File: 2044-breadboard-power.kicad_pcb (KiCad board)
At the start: 2 copper layers, 51 x 22 mm, 13 parts, among them J1 Conn_02x02_Odd_Even, J2 PJ-102AH, J3 Conn_02x02_Odd_Even, U1 AZ1117CH-3.3TRG1, U2 AZ1117CH-5.0TRG1

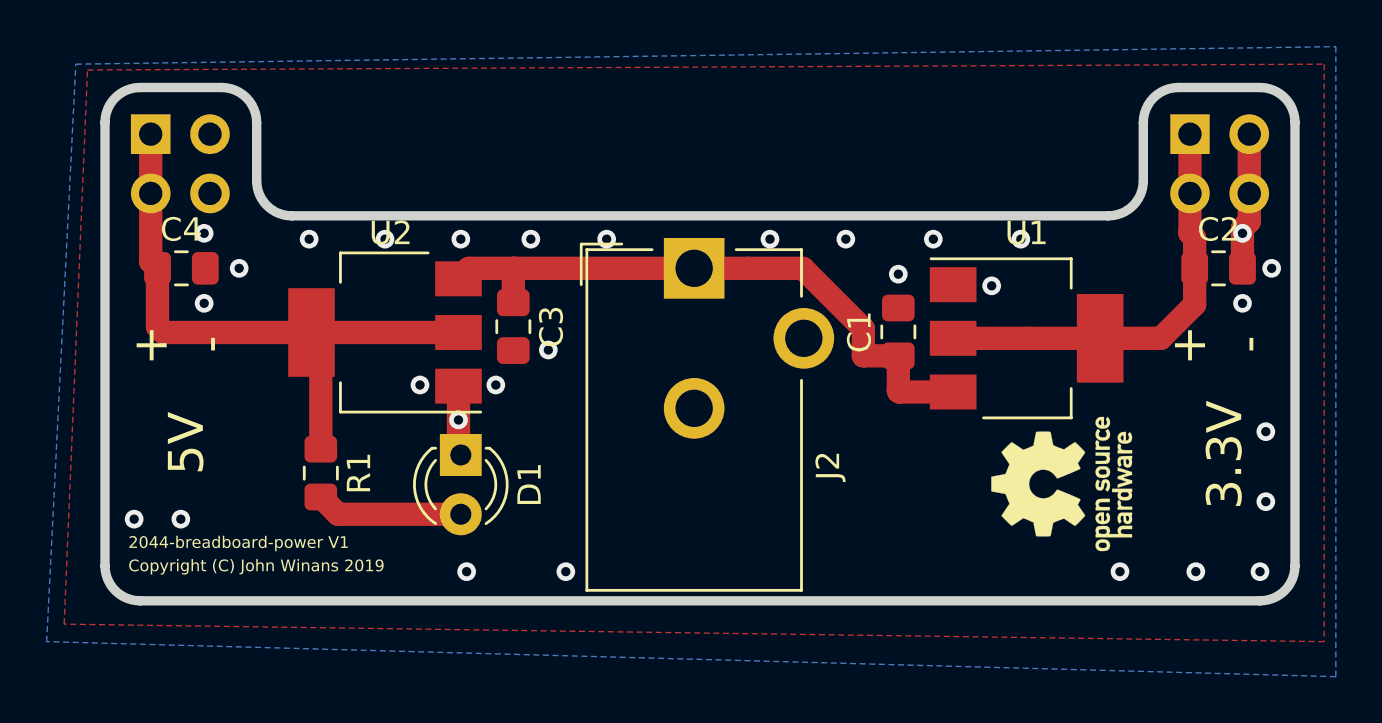
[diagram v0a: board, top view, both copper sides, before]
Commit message: Add ground on the output headers.
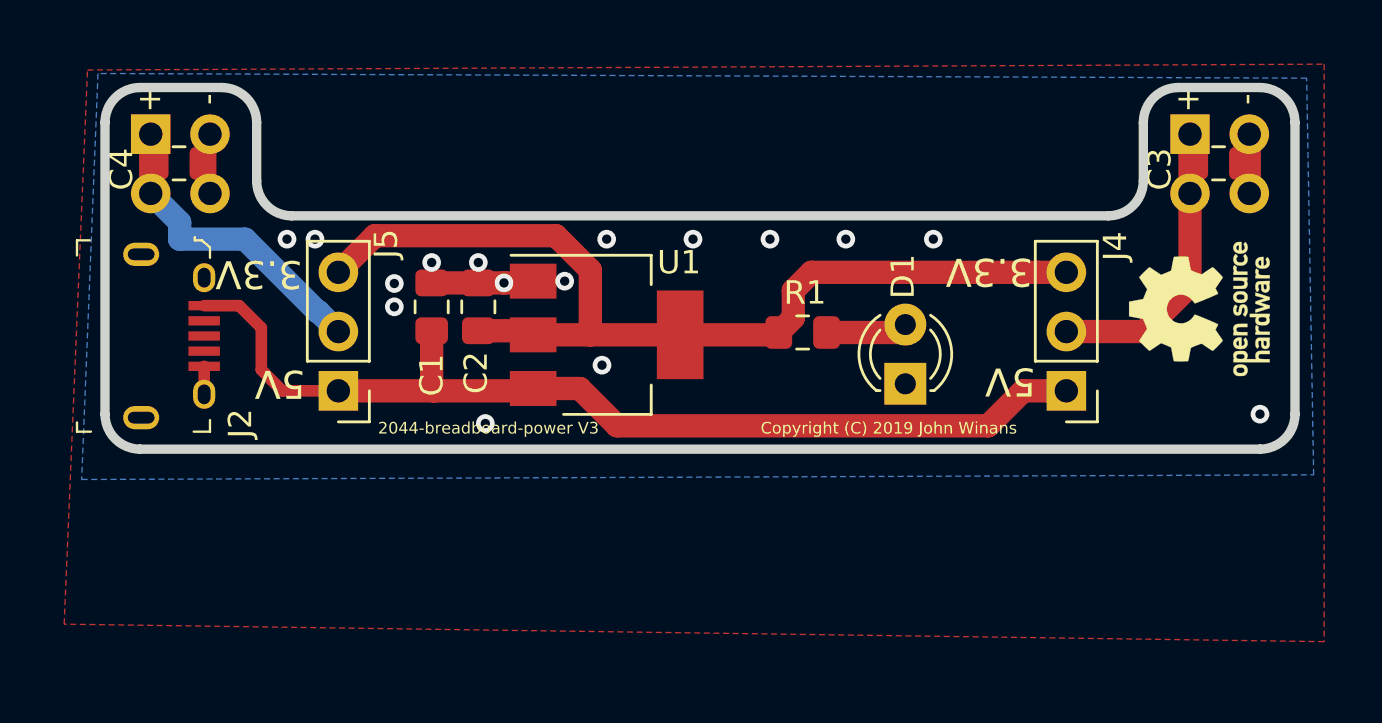
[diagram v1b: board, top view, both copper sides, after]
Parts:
- removed the REF** at (159.5, 72.8)
- removed U2: AZ1117CH-5.0TRG1, Package_TO_SOT_SMD:SOT-223-3_TabPin2
- added J4: Conn_01x03, Connector_PinHeader_2.54mm:PinHeader_1x03_P2.54mm_Vertical, F.Cu at (156.7, 74.0)
- added J5: Conn_01x03, Connector_PinHeader_2.54mm:PinHeader_1x03_P2.54mm_Vertical, F.Cu at (125.5, 74.0)
- C3: value 10uF -> 22uF
- J2: value PJ-102AH -> 10118194-0001LF; footprint Connector_BarrelJack:BarrelJack_CUI_PJ-102AH_Horizontal -> digikey-footprints:USB_Micro_B_Female_10118194-0001LF
- R1: value 1K -> 330
- moved C2 31.8 mm to (131.5, 70.4), turned to 90 degrees
- moved C3 31.0 mm to (163.2, 64.2), turned to 0 degrees
- moved R1 21.5 mm to (145.4, 71.5), turned to 0 degrees
- moved J2 21.2 mm to (119.8, 71.7), turned to 270 degrees
- moved C1 20.0 mm to (129.5, 70.4)
- moved D1 19.3 mm to (149.8, 73.7), turned to 90 degrees
- moved U1 18.0 mm to (137.0, 71.6)
- moved REF** 9.54 mm to (162.4, 70.5)
- moved C4 4.50 mm to (118.7, 64.2)
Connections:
- C1 pad 1: Net-(C1-Pad1) -> +5V
- C2 pad 1: Net-(C2-Pad1) -> +3V3
- C3 pad 1: Net-(C1-Pad1) -> /Vout1
- C4 pad 1: Net-(C4-Pad1) -> /Vout2
- J1 pad 1: Net-(C2-Pad1) -> /Vout1
- J1 pad 2: Net-(C2-Pad1) -> /Vout1
- J2 pad 1: Net-(C1-Pad1) -> +5V
- J2 pad 2: GND -> Net-(J2-Pad2)
- J2 pad 3: (no net) -> Net-(J2-Pad3)
- J3 pad 1: Net-(C4-Pad1) -> /Vout2
- J3 pad 2: Net-(C4-Pad1) -> /Vout2
- R1 pad 1: Net-(C4-Pad1) -> +3V3
- U1 pad 2: Net-(C2-Pad1) -> +3V3
- U1 pad 3: Net-(C1-Pad1) -> +5V
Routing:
- net +5V: track 0.00 -> 43.5 mm
- net +3V3: track 0.00 -> 41.9 mm
- net Net-(C1-Pad1): track 26.6 -> 0.00 mm
- net Net-(C4-Pad1): track 26.5 -> 0.00 mm
- net Net-(C2-Pad1): track 18.3 -> 0.00 mm
- net /Vout2: track 0.00 -> 13.5 mm
- net /Vout1: track 0.00 -> 12.6 mm
- net Net-(D1-Pad2): track 6.31 -> 3.52 mm
- net GND: track 8.86 -> 10.9 mm, vias 30 -> 16
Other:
- board size 51 x 22 mm -> 51 x 15.5 mm
- board text added: "2044-breadboard-power V3"
- board text added: "Copyright (C) 2019 John Winans"
- board text removed: "2044-breadboard-power V1"
- board text removed: "Copyright (C) John Winans 2019"
